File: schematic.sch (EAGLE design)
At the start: 40 parts, among them CN1 1X4-BIG, CN2 1X4-BIG, IC3 78TO220, IC4 78TO220

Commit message: Initial board layout
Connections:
- net CTRL_A_3V3: now also U$1.D5; no longer U$1.D4
- net CTRL_B_3V3: now also U$1.D4; no longer U$1.D5
- net CTRL_G: now also U$1.D3; no longer U$1.D2
- net CTRL_R: now also U$1.D2; no longer U$1.D3
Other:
- moved on the sheet: C1, C2, C3, C4, C5, C6, CN1, CN2, IC3, IC4, LED1, OK1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

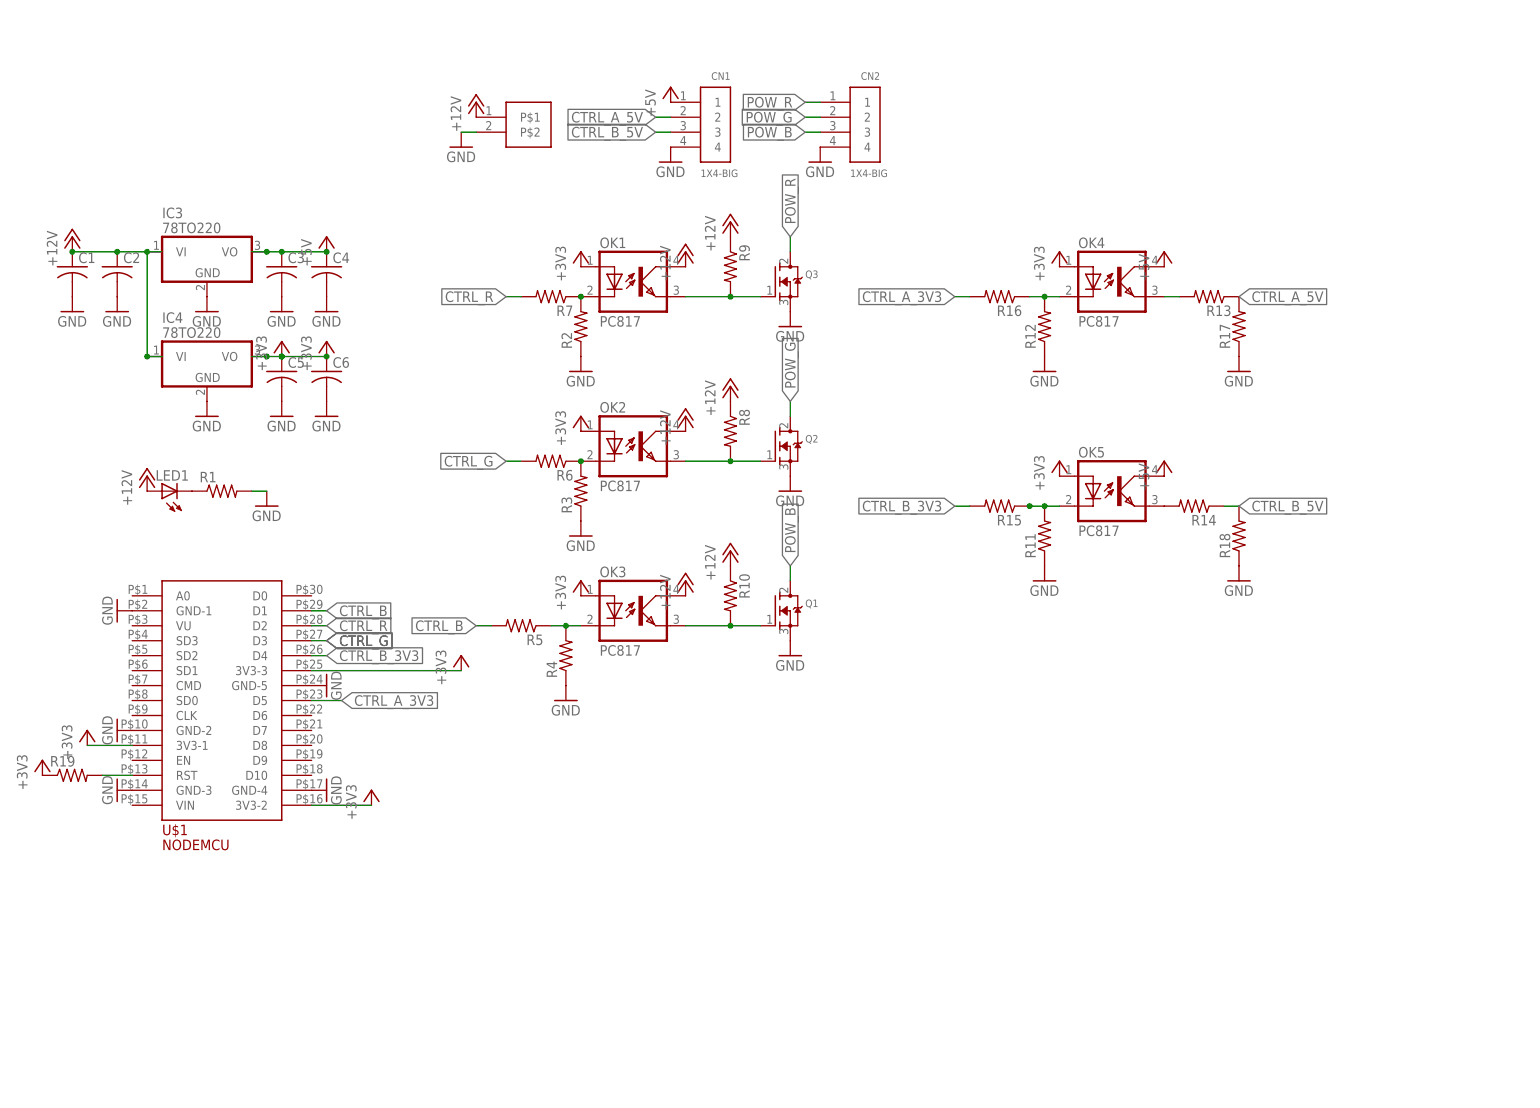
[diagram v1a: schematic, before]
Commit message: Inverted polarity of LED control on optocouplers
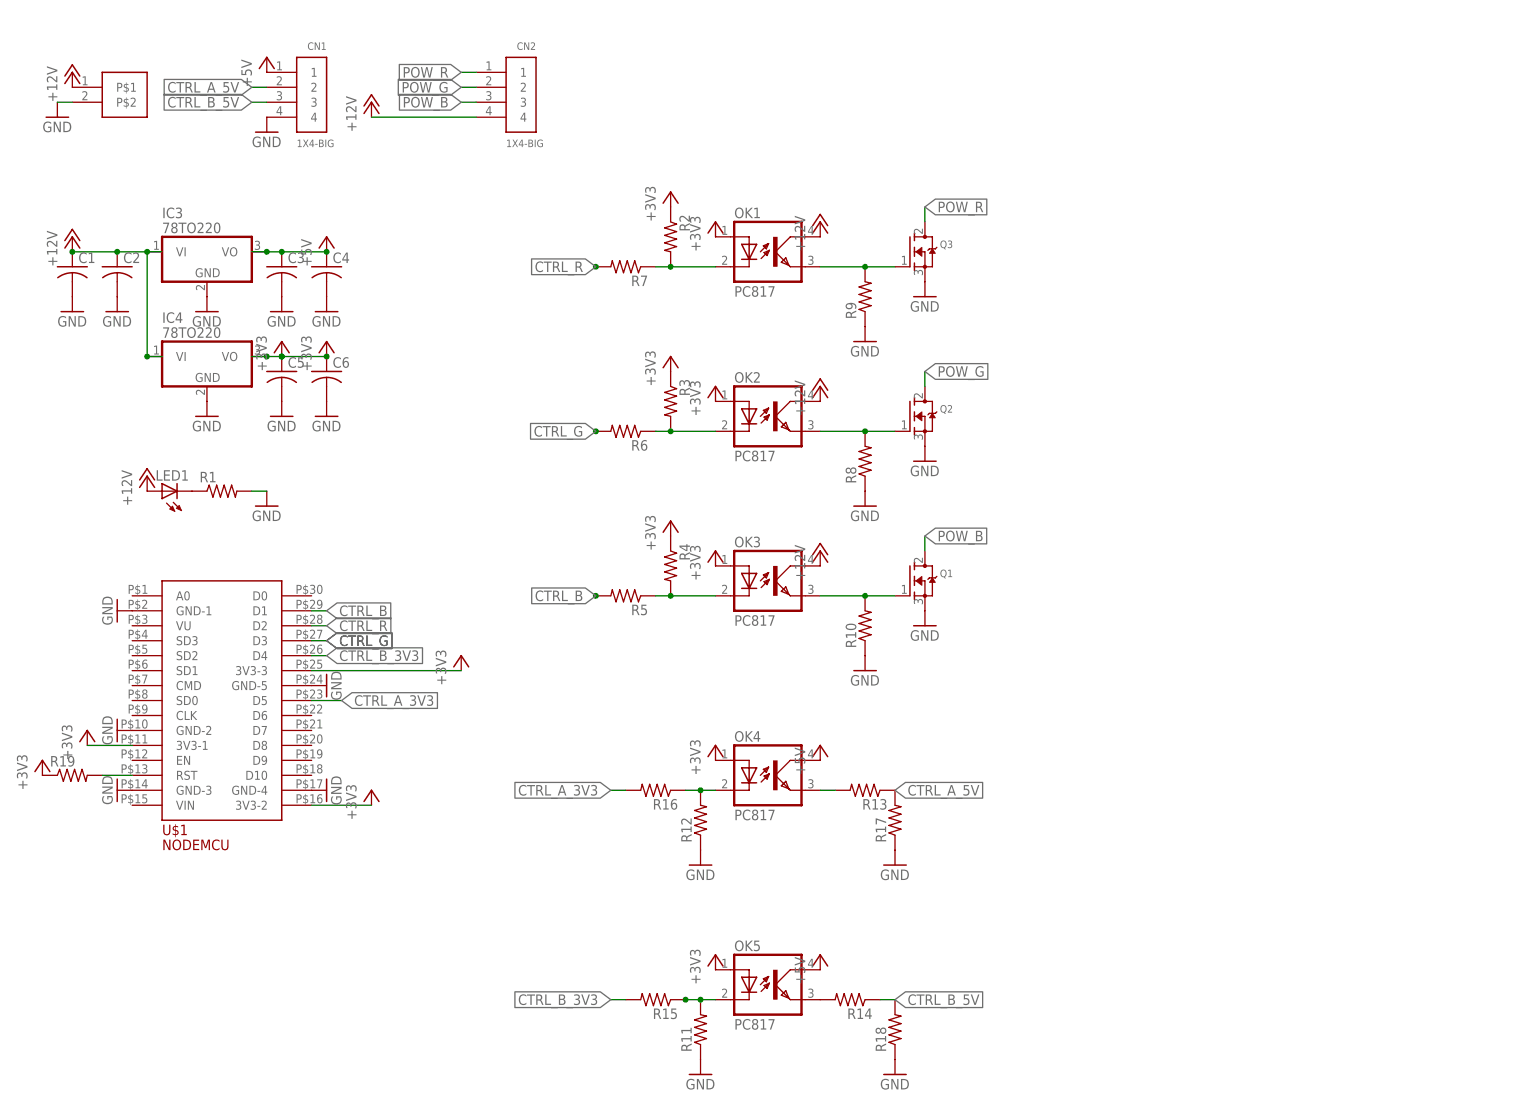
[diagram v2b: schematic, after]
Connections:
- net +12V: now also CN2.4; no longer R10.1, R8.1, R9.1
- net GND: now also R9.1; no longer CN2.4, R2.1, R3.1, R4.1
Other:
- moved on the sheet: CN1, CN2, OK1, OK2, OK3, OK4, OK5, Q1, Q2, Q3, R10, R11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

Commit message: Updated board; enhanced schematics organization
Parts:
- R1, R13, R14, R15, R16, R19, R5, R6, R7: value (none) -> 1k
- R10, R11, R12, R17, R18, R2, R3, R4, R8, R9: value (none) -> 10k
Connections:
- net +3V3: now also R2.1, R3.1, R4.1
- net GND: now also R10.1, R8.1
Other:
- note added: "5V and 3V3 power regulators"
- note added: "5V controllers"
- note added: "5V controllers connector"
- note added: "LED power control"
- note added: "Power connector"
- note added: "RGB LED strip connector"
- moved on the sheet: OK4, R12, R13, R16, R17
